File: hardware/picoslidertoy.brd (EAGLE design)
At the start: 152.4 x 50.8 mm, 32 parts, among them U2 RASPBERRY_PICOSMD

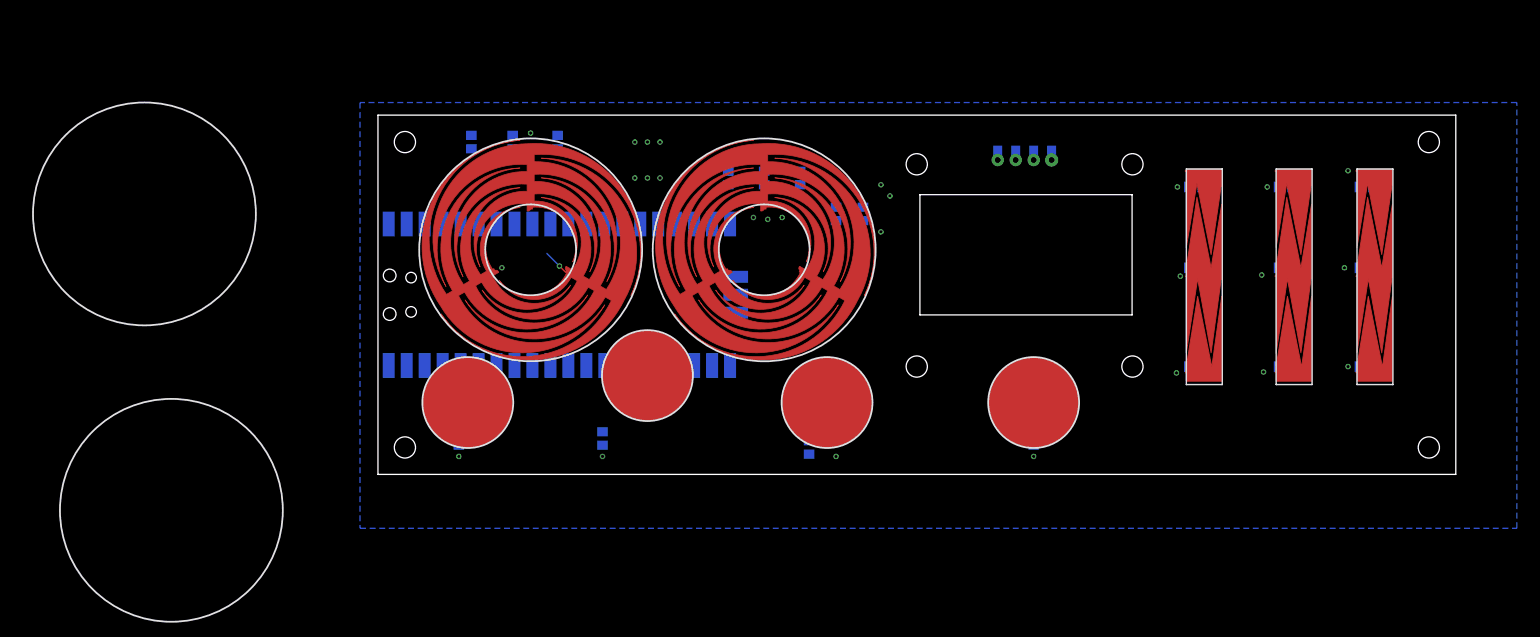
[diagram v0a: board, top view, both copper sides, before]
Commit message: picoslidertoy layout mostly done
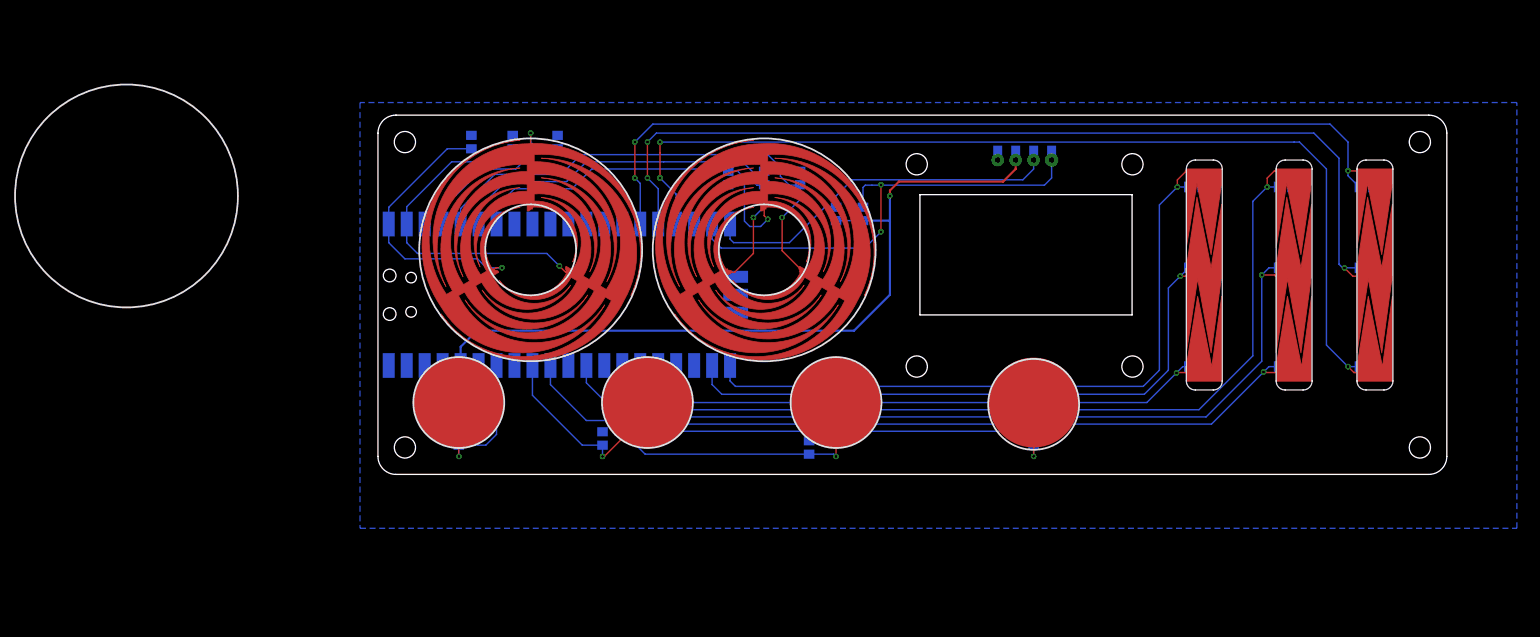
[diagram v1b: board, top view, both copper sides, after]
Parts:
- moved TP2 3.81 mm to (38.1, -40.6)
- moved TP1 1.27 mm to (11.4, -40.6)
- moved TP3 1.27 mm to (64.8, -40.6)
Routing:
- net SLIDEC1: track 0.00 -> 140.8 mm
- net SLIDEC2: track 0.00 -> 132.3 mm
- net SLIDEC3: track 0.00 -> 123.1 mm
- net SLIDEB1: track 0.00 -> 120.7 mm
- net SLIDEB2: track 0.00 -> 112.8 mm
- net +3V3: track 0.00 -> 109.8 mm
- net SLIDEB3: track 0.00 -> 103.0 mm
- net SLIDEA1: track 0.00 -> 95.5 mm
- net SLIDEA2: track 0.00 -> 85.7 mm
- net SLIDEA3: track 0.00 -> 79.7 mm
- net TPAD4: track 0.00 -> 78.7 mm
- net ROTB1: track 0.00 -> 70.6 mm
- net SDA: track 0.00 -> 67.8 mm
- net ROTB2: track 0.00 -> 62.9 mm
- net TPAD3: track 0.00 -> 54.9 mm
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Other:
- board size 152.4 x 50.8 mm -> 151.1 x 50.8 mm

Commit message: old picoslidertoy sync up, but moved dev to its own repo and kicad
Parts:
- added 3V3, GND, GP6, GP7, GP8, GP9: TPTP20R, testpad:TP20R
- R1, R10, R11, R12, R13, R14, R15, R16, R17, R18, R19, R2, R3, R4, R5, R6, R7, R8, R9: value (none) -> 1M
- R20, R21: value (none) -> 4.7k
- SLIDER1, SLIDER2, SLIDER3: value TOUCHSLIDER36X30 -> TOUCHSLIDER36X40; device todstuff2023:TOUCHSLIDER3_6X30 -> todstuff2023:TOUCHSLIDER3_6X40
- SMDBACK2: value 13"OLED -> 13"OLEDSMDONLY; device 13oled:1.3"OLED_SMDBACK -> 13oled:1.3"OLED_SMDBACKONLY
- moved R16 62.7 mm to (11.4, -47.0)
- moved R19 61.0 mm to (92.7, -47.0)
- moved R18 53.4 mm to (64.8, -47.0)
- moved R17 49.5 mm to (31.8, -47.0)
- moved R21 39.9 mm to (68.6, -14.0), turned to 90 degrees
- moved R20 33.2 mm to (64.8, -14.0)
- moved SLIDER1 3.59 mm to (111.8, -5.08)
- moved SLIDER2 2.84 mm to (125.7, -5.08)
- moved R9 2.84 mm to (113.0, -34.3)
- moved R7 2.84 mm to (113.0, -8.89)
- moved R8 2.84 mm to (113.0, -20.3)
- moved SLIDER3 2.84 mm to (139.7, -5.08)
- moved TP3 2.54 mm to (67.3, -40.6)
- moved R4 2.54 mm to (52.1, -8.89)
- moved R5 2.54 mm to (57.1, -8.89)
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- renumbered U2 to U1
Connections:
- new net N$1: GP6.TP, U1.P$9
- new net N$2: GP7.TP, U1.P$10
- new net N$3: GP9.TP, U1.P$12
- new net N$4: GP8.TP, U1.P$11
- net +3V3: now also 3V3.TP, R20.2, R21.2; no longer R16.2, R17.2, SMDBACK2.VCC_2
- net GND: now also GND.TP, R16.1, R17.1; no longer R20.1, R21.1, SMDBACK2.GND_2
- net SCL: now also R20.1; no longer R16.1, SMDBACK2.SCL_2
- net SDA: now also R21.1; no longer R17.1, SMDBACK2.SDA_2
- net TPAD1: now also R16.2; no longer R18.2
- net TPAD2: now also R17.2; no longer R19.2
- net TPAD3: now also R18.2; no longer R20.2
- net TPAD4: now also R19.2; no longer R21.2
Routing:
- net +3V3: track 109.8 -> 127.6 mm, vias 1 -> 2
- net SLIDEC1: track 140.8 -> 150.2 mm
- net SDA: track 67.8 -> 59.3 mm
- net SLIDEB3: track 103.0 -> 111.4 mm
- net SLIDEA3: track 79.7 -> 86.5 mm
- net SLIDEA1: track 95.5 -> 89.5 mm
- net SLIDEC2: track 132.3 -> 137.6 mm
- net SLIDEB2: track 112.8 -> 116.5 mm
- net ROTB2: track 62.9 -> 66.5 mm
- net ROTA1: track 37.6 -> 34.3 mm
- net N$4: track 0.00 -> 3.21 mm
- net N$3: track 0.00 -> 3.21 mm
- net N$2: track 0.00 -> 3.21 mm
- net N$1: track 0.00 -> 3.21 mm
- net ROTB1: track 70.6 -> 73.4 mm
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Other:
- board size 151.1 x 50.8 mm -> 152.4 x 50.8 mm
- board text added: "@todbot"
- board text added: "D C + -"
- board text added: "DISP1"
- board text added: "U1: Raspberry Pi Pico DISP1: 1.3" I2C OLED R1-R19 : 1M R20-R21: 4.7k optional"
- board text added: "github.com/todbot/touchwheels for code and design files 28 Nov 2023 - picoslidertoy - @todbot"
- board text added: "picoslidertoy"
- board text removed: "R1-R3 : 1M"
- board text removed: "github.com/todbot/touchwheels for code and design files 27 Oct 2023 - touchwheel0 - @todbot"
